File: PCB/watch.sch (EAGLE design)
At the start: 61 parts, among them IC1 ISL1209, J2 USB-MICROB, Q1 32.768 KHz, T1 BC850, U2 MKL27Z256VLH4

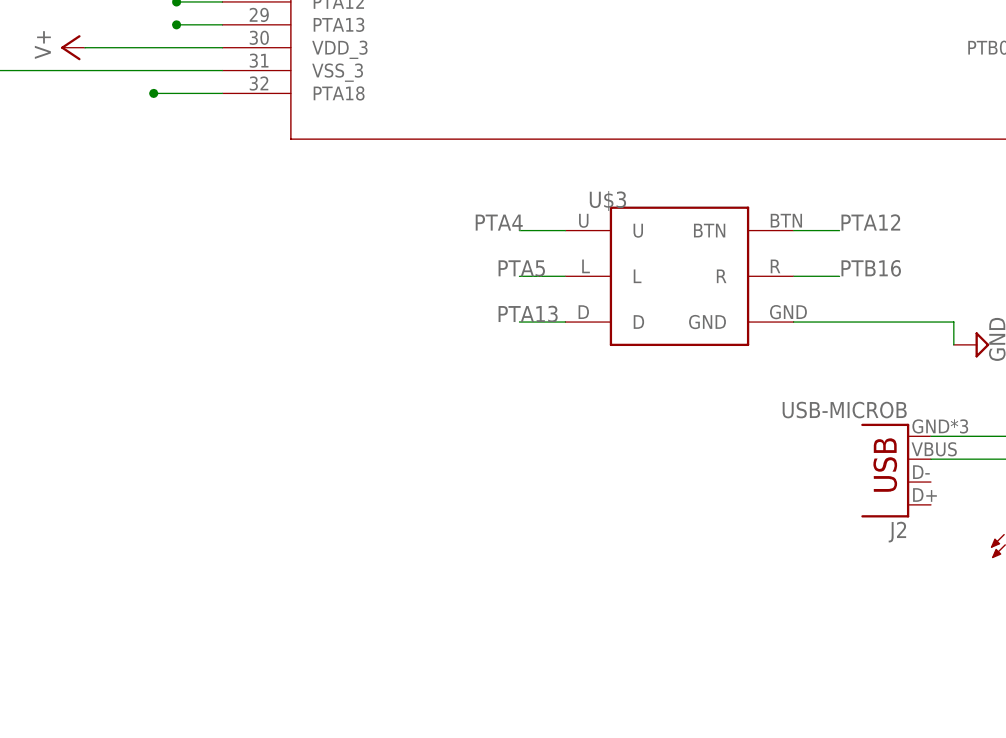
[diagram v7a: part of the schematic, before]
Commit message: added control switch resistors
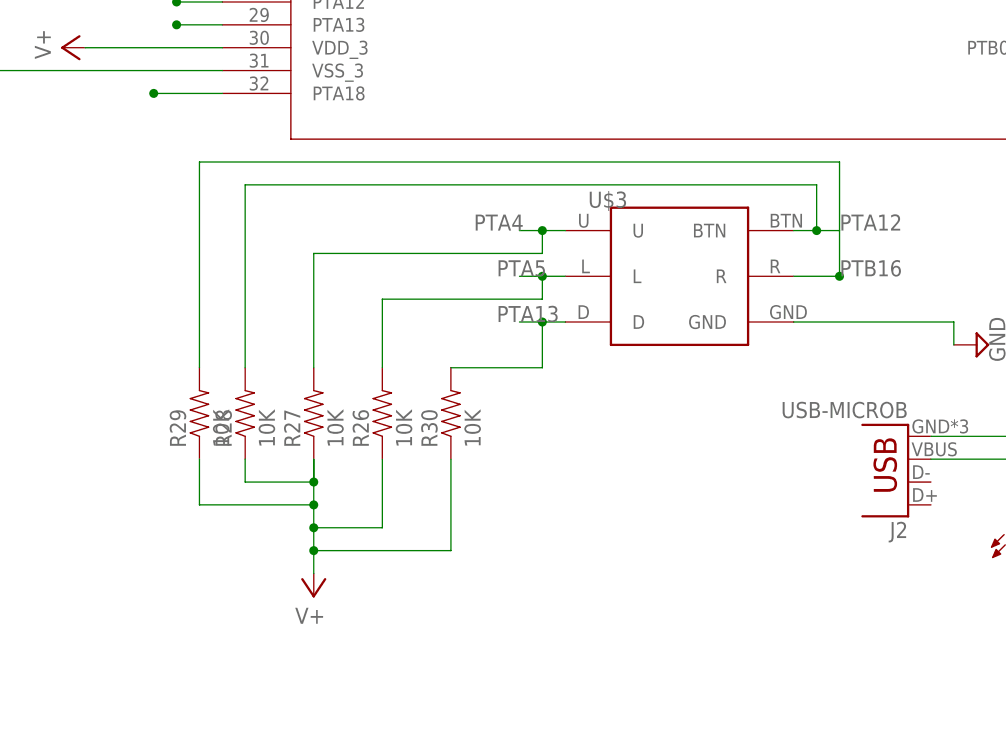
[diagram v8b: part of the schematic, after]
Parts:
- added R26, R27, R28, R29, R30: 10K, SparkFun-Resistors:RESISTOR0603
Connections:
- net PTA12: now also R28.2
- net PTA13: now also R30.2
- net PTA4: now also R27.2
- net PTA5: now also R26.2
- net PTB16: now also R29.2
- net V+: now also R26.1, R27.1, R28.1, R29.1, R30.1
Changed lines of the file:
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@@
 <part name="R25" library="SparkFun-Resistors" deviceset="RESISTOR" device="0603" value="220Ohm"/>
 <part name="R19" library="SparkFun-Resistors" deviceset="RESISTOR" device="0603" value="220Ohm"/>
+<part name="R26" library="SparkFun-Resistors" deviceset="RESISTOR" device="0603" value="10K"/>
+<part name="R27" library="SparkFun-Resistors" deviceset="RESISTOR" device="0603" value="10K"/>
+<part name="R28" library="SparkFun-Resistors" deviceset="RESISTOR" device="0603" value="10K"/>
+<part name="R29" library="SparkFun-Resistors" deviceset="RESISTOR" device="0603" value="10K"/>
+<part name="R30" library="SparkFun-Resistors" deviceset="RESISTOR" device="0603" value="10K"/>
+<part name="SUPPLY41" library="supply2" deviceset="V+" device=""/>
 </parts>
 <sheets>
@@
 <instance part="R25" gate="G$1" x="-12.7" y="276.86" rot="R270"/>
 <instance part="R19" gate="G$1" x="-17.78" y="264.16" rot="R90"/>
+<instance part="R26" gate="G$1" x="-7.62" y="48.26" rot="R90"/>
+<instance part="R27" gate="G$1" x="-15.24" y="48.26" rot="R90"/>
+<instance part="R28" gate="G$1" x="-22.86" y="48.26" rot="R90"/>
+<instance part="R29" gate="G$1" x="-27.94" y="48.26" rot="R90"/>
+<instance part="R30" gate="G$1" x="0" y="48.26" rot="R90"/>
+<instance part="SUPPLY41" gate="1" x="-15.24" y="27.94" rot="R180"/>
 </instances>
 <busses>
@@
 <junction x="129.54" y="200.66"/>
 </segment>
+<segment>
+<pinref part="R27" gate="G$1" pin="1"/>
+<pinref part="SUPPLY41" gate="1" pin="V+"/>
+<wire x1="-15.24" y1="43.18" x2="-15.24" y2="40.64" width="0.1524" layer="91"/>
+<pinref part="R28" gate="G$1" pin="1"/>
+<wire x1="-15.24" y1="40.64" x2="-15.24" y2="38.1" width="0.1524" layer="91"/>
+<wire x1="-15.24" y1="38.1" x2="-15.24" y2="35.56" width="0.1524" layer="91"/>
+<wire x1="-15.24" y1="35.56" x2="-15.24" y2="33.02" width="0.1524" layer="91"/>
+<wire x1="-15.24" y1="33.02" x2="-15.24" y2="30.48" width="0.1524" layer="91"/>
+<wire x1="-22.86" y1="43.18" x2="-22.86" y2="40.64" width="0.1524" layer="91"/>
+<wire x1="-22.86" y1="40.64" x2="-15.24" y2="40.64" width="0.1524" layer="91"/>
+<wire x1="-15.24" y1="40.64" x2="-15.24" y2="43.18" width="0.1524" layer="91"/>
+<pinref part="R29" gate="G$1" pin="1"/>
+<wire x1="-27.94" y1="43.18" x2="-27.94" y2="38.1" width="0.1524" layer="91"/>
+<wire x1="-27.94" y1="38.1" x2="-15.24" y2="38.1" width="0.1524" layer="91"/>
+<pinref part="R26" gate="G$1" pin="1"/>
+<wire x1="-7.62" y1="43.18" x2="-7.62" y2="35.56" width="0.1524" layer="91"/>
+<wire x1="-7.62" y1="35.56" x2="-15.24" y2="35.56" width="0.1524" layer="91"/>
+<pinref part="R30" gate="G$1" pin="1"/>
+<wire x1="0" y1="43.18" x2="0" y2="33.02" width="0.1524" layer="91"/>
+<wire x1="0" y1="33.02" x2="-15.24" y2="33.02" width="0.1524" layer="91"/>
+<junction x="-15.24" y="38.1"/>
+<junction x="-15.24" y="40.64"/>
+<junction x="-15.24" y="35.56"/>
+<junction x="-15.24" y="33.02"/>
+</segment>
 </net>
 <net name="PTA19" class="0">
@@
 <segment>
 <pinref part="U$3" gate="G$1" pin="D"/>
-<wire x1="12.7" y1="58.42" x2="7.62" y2="58.42" width="0.1524" layer="91"/>
+<wire x1="12.7" y1="58.42" x2="10.16" y2="58.42" width="0.1524" layer="91"/>
 <label x="5.08" y="58.42" size="1.778" layer="95"/>
+<pinref part="R30" gate="G$1" pin="2"/>
+<wire x1="10.16" y1="58.42" x2="7.62" y2="58.42" width="0.1524" layer="91"/>
+<wire x1="0" y1="53.34" x2="10.16" y2="53.34" width="0.1524" layer="91"/>
+<wire x1="10.16" y1="53.34" x2="10.16" y2="58.42" width="0.1524" layer="91"/>
+<junction x="10.16" y="58.42"/>
 </segment>
 <segment>
@@
 <segment>
 <pinref part="U$3" gate="G$1" pin="L"/>
-<wire x1="12.7" y1="63.5" x2="7.62" y2="63.5" width="0.1524" layer="91"/>
+<wire x1="12.7" y1="63.5" x2="10.16" y2="63.5" width="0.1524" layer="91"/>
 <label x="5.08" y="63.5" size="1.778" layer="95"/>
+<pinref part="R26" gate="G$1" pin="2"/>
+<wire x1="10.16" y1="63.5" x2="7.62" y2="63.5" width="0.1524" layer="91"/>
+<wire x1="-7.62" y1="53.34" x2="-7.62" y2="60.96" width="0.1524" layer="91"/>
+<wire x1="-7.62" y1="60.96" x2="10.16" y2="60.96" width="0.1524" layer="91"/>
+<wire x1="10.16" y1="60.96" x2="10.16" y2="63.5" width="0.1524" layer="91"/>
+<junction x="10.16" y="63.5"/>
 </segment>
 <segment>
@@
 <segment>
 <pinref part="U$3" gate="G$1" pin="U"/>
-<wire x1="12.7" y1="68.58" x2="7.62" y2="68.58" width="0.1524" layer="91"/>
+<wire x1="12.7" y1="68.58" x2="10.16" y2="68.58" width="0.1524" layer="91"/>
 <label x="2.54" y="68.58" size="1.778" layer="95"/>
+<pinref part="R27" gate="G$1" pin="2"/>
+<wire x1="10.16" y1="68.58" x2="7.62" y2="68.58" width="0.1524" layer="91"/>
+<wire x1="-15.24" y1="53.34" x2="-15.24" y2="66.04" width="0.1524" layer="91"/>
+<wire x1="-15.24" y1="66.04" x2="10.16" y2="66.04" width="0.1524" layer="91"/>
+<wire x1="10.16" y1="66.04" x2="10.16" y2="68.58" width="0.1524" layer="91"/>
+<junction x="10.16" y="68.58"/>
 </segment>
 <segment>
@@
 <wire x1="38.1" y1="63.5" x2="43.18" y2="63.5" width="0.1524" layer="91"/>
 <label x="43.18" y="63.5" size="1.778" layer="95"/>
+<pinref part="R29" gate="G$1" pin="2"/>
+<wire x1="-27.94" y1="53.34" x2="-27.94" y2="76.2" width="0.1524" layer="91"/>
+<wire x1="-27.94" y1="76.2" x2="43.18" y2="76.2" width="0.1524" layer="91"/>
+<wire x1="43.18" y1="76.2" x2="43.18" y2="63.5" width="0.1524" layer="91"/>
+<junction x="43.18" y="63.5"/>
 </segment>
 <segment>
@@
 <segment>
 <pinref part="U$3" gate="G$1" pin="BTN"/>
-<wire x1="38.1" y1="68.58" x2="43.18" y2="68.58" width="0.1524" layer="91"/>
+<wire x1="38.1" y1="68.58" x2="40.64" y2="68.58" width="0.1524" layer="91"/>
 <label x="43.18" y="68.58" size="1.778" layer="95"/>
-</segment>
-<segment>
+<pinref part="R28" gate="G$1" pin="2"/>
+<wire x1="40.64" y1="68.58" x2="43.18" y2="68.58" width="0.1524" layer="91"/>
+<wire x1="-22.86" y1="53.34" x2="-22.86" y2="73.66" width="0.1524" layer="91"/>
+<wire x1="-22.86" y1="73.66" x2="40.64" y2="73.66" width="0.1524" layer="91"/>
+<wire x1="40.64" y1="73.66" x2="40.64" y2="68.58" width="0.1524" layer="91"/>
+<junction x="40.64" y="68.58"/>
+</segment>
+<segment>
